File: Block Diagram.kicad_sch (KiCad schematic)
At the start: 48 parts, among them J1001 Header, J701 ZHOURI DC3, J801 Molex 430452427, J901 Header

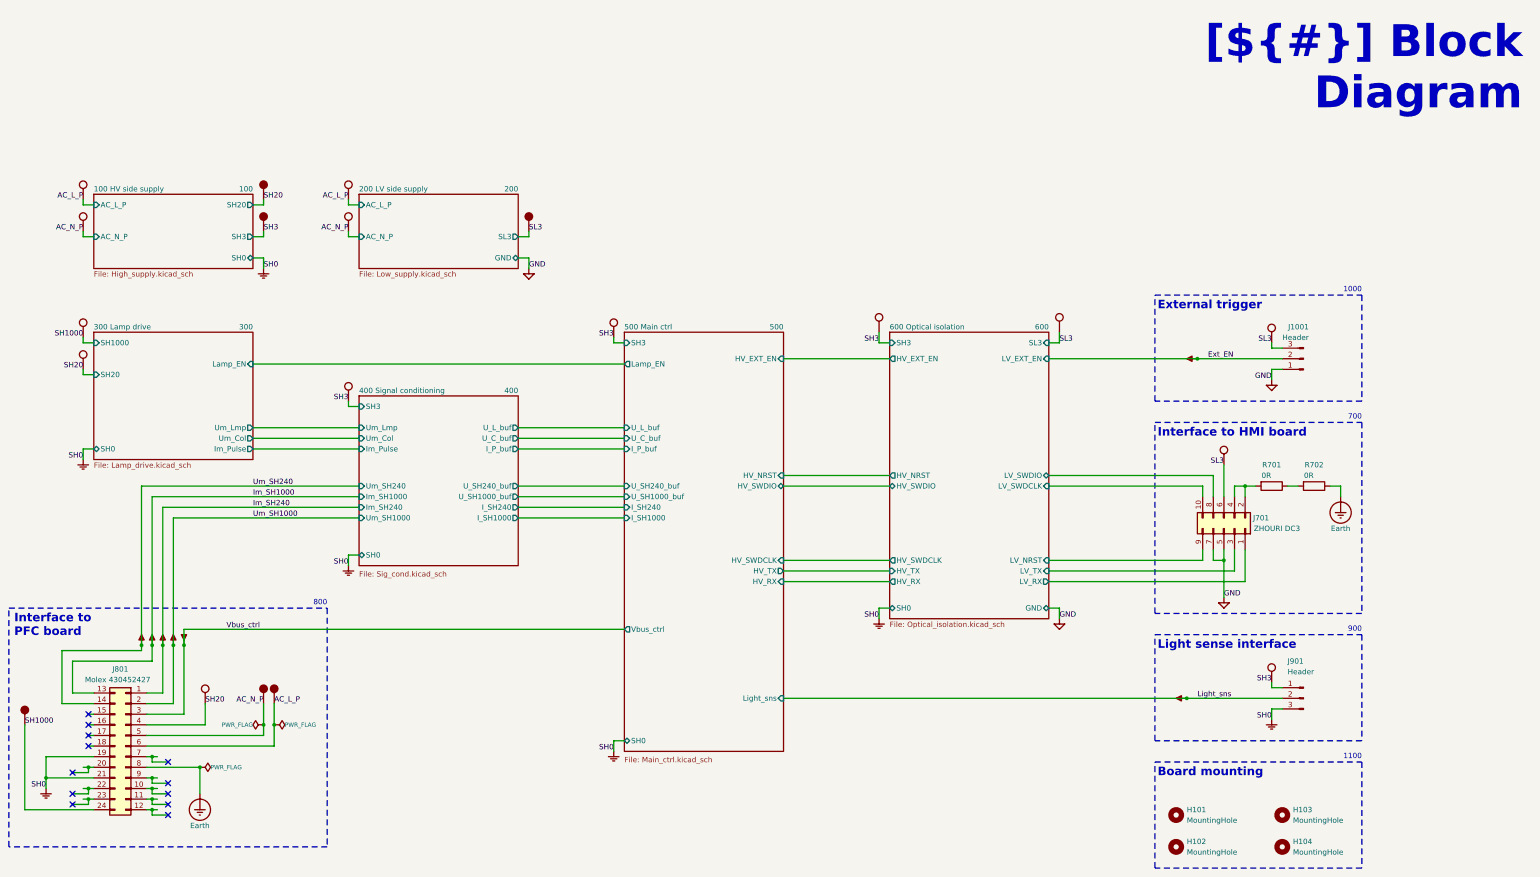
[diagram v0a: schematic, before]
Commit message: Reworked sheet titles
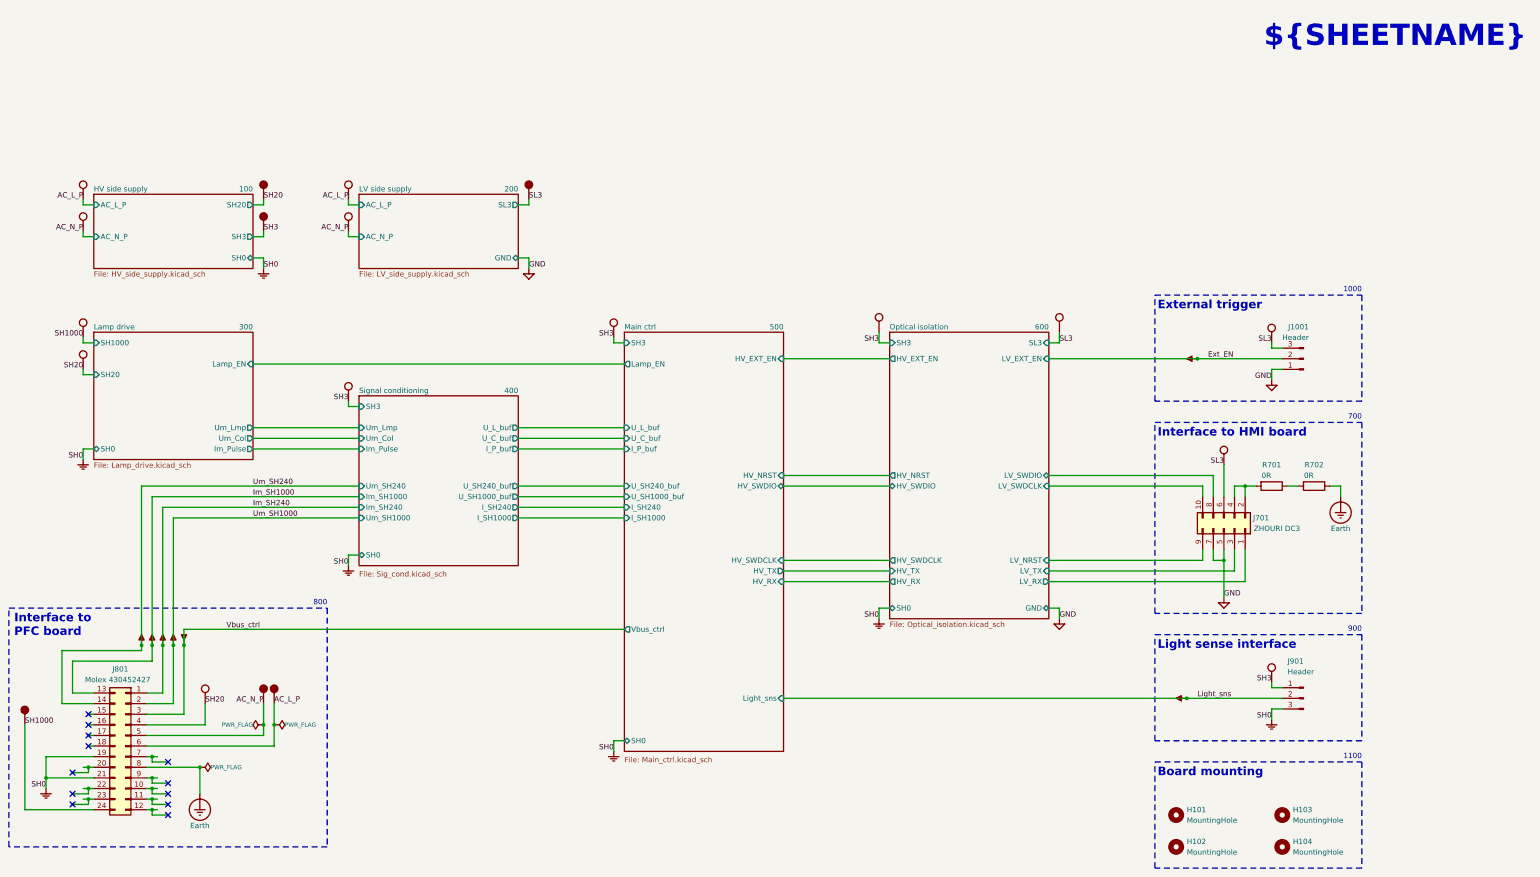
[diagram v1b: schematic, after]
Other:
- sheet 100 HV side supply renamed HV side supply
- sheet 200 LV side supply renamed LV side supply
- sheet 300 Lamp drive renamed Lamp drive
- sheet 400 Signal conditioning renamed Signal conditioning
- sheet 500 Main ctrl renamed Main ctrl
- sheet 600 Optical isolation renamed Optical isolation
- sheet HV side supply: file High_supply.kicad_sch -> HV_side_supply.kicad_sch
- sheet LV side supply: file Low_supply.kicad_sch -> LV_side_supply.kicad_sch
- title: Block Diagram -> ${SHEETNAME}
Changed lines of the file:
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@@
 	(paper "A3")
 	(title_block
-		(title "Block Diagram")
+		(title "${SHEETNAME}")
 		(date "2025-01-12")
 		(rev "${REVISION}")
@@
 		)
 	)
-	(text_box "[${#}] ${TITLE}"
+	(text_box "${SHEETNAME}"
 		(exclude_from_sim no)
-		(at 304.8 20.32 0)
-		(size 101.6 12.7)
-		(margins 5.9999 5.9999 5.9999 5.9999)
+		(at 350.52 15.24 0)
+		(size 53.34 7.62)
+		(margins 2.54 1.27 2.54 1.27)
 		(stroke
 			(width -0.0001)
@@
 			(font
 				(face "Times New Roman")
-				(size 7.62 7.62)
+				(size 5.08 5.08)
 				(thickness 1.2)
 				(bold yes)
@@
 	(wire
 		(pts
-			(xy 160.02 67.31) (xy 162.56 67.31)
+			(xy 160.02 59.69) (xy 162.56 59.69)
 		)
 		(stroke
@@
 	(wire
 		(pts
-			(xy 162.56 66.04) (xy 162.56 67.31)
+			(xy 162.56 58.42) (xy 162.56 59.69)
 		)
 		(stroke
@@
 	)
 	(label "SL3"
-		(at 162.56 66.04 0)
+		(at 162.56 58.42 0)
 		(effects
 			(font
@@
 	(symbol
 		(lib_id "personal:Cosmetic_PWR_SRC")
-		(at 162.56 66.04 0)
+		(at 162.56 58.42 0)
 		(mirror y)
 		(unit 1)
@@
 		(fields_autoplaced yes)
 		(property "Reference" "P787"
-			(at 162.56 60.706 0)
+			(at 162.56 53.086 0)
 			(do_not_autoplace yes)
 			(effects
@@
 		)
 		(property "Value" "~"
-			(at 162.56 59.69 90)
+			(at 162.56 52.07 90)
 			(effects
 				(font
@@
 		)
 		(property "Footprint" ""
-			(at 162.56 66.04 0)
+			(at 162.56 58.42 0)
 			(effects
 				(font
@@
 		)
 		(property "Datasheet" ""
-			(at 162.56 66.04 0)
+			(at 162.56 58.42 0)
 			(effects
 				(font
@@
 		)
 		(property "Description" ""
-			(at 162.56 66.04 0)
+			(at 162.56 58.42 0)
 			(effects
 				(font
@@
 			(color 255 220 210 1.0000)
 		)
-		(property "Sheetname" "400 Signal conditioning"
+		(property "Sheetname" "Signal conditioning"
 			(at 121.92 104.14 0)
 			(effects
@@
 			)
 		)
-		(property "Range" "400"
+		(property "RefDes" "400"
 			(at 160.02 104.14 0)
 			(effects
@@
 			(color 255 220 210 1.0000)
 		)
-		(property "Sheetname" "300 Lamp drive"
+		(property "Sheetname" "Lamp drive"
 			(at 58.42 88.9 0)
 			(effects
@@
 			)
 		)
-		(property "Range" "300"
+		(property "RefDes" "300"
 			(at 96.52 88.9 0)
 			(effects
@@
 			(color 255 220 210 1.0000)
 		)
-		(property "Sheetname" "600 Optical isolation"
+		(property "Sheetname" "Optical isolation"
 			(at 248.92 88.9 0)
 			(effects
@@
 			)
 		)
-		(property "Range" "600"
+		(property "RefDes" "600"
 			(at 287.02 88.9 0)
 			(effects
@@
 			(color 255 220 210 1.0000)
 		)
-		(property "Sheetname" "200 LV side supply"
+		(property "Sheetname" "LV side supply"
 			(at 121.92 55.88 0)
 			(effects
@@
 			)
 		)
-		(property "Sheetfile" "Low_supply.kicad_sch"
+		(property "Sheetfile" "LV_side_supply.kicad_sch"
 			(at 121.92 75.5146 0)
 			(effects
@@
 			)
 		)
-		(property "Range" "200"
+		(property "RefDes" "200"
 			(at 160.02 55.88 0)
 			(effects
@@
 		)
 		(pin "SL3" output
-			(at 160.02 67.31 0)
+			(at 160.02 59.69 0)
 			(effects
 				(font
@@
 			(color 255 220 210 1.0000)
 		)
-		(property "Sheetname" "100 HV side supply"
+		(property "Sheetname" "HV side supply"
 			(at 58.42 55.88 0)
 			(effects
@@
 			)
 		)
-		(property "Sheetfile" "High_supply.kicad_sch"
+		(property "Sheetfile" "HV_side_supply.kicad_sch"
 			(at 58.42 75.5146 0)
 			(effects
@@
 			)
 		)
-		(property "Range" "100"
+		(property "RefDes" "100"
 			(at 96.52 55.88 0)
 			(effects
@@
 			(color 255 220 210 1.0000)
 		)
-		(property "Sheetname" "500 Main ctrl"
+		(property "Sheetname" "Main ctrl"
 			(at 185.42 88.9 0)
 			(effects
@@
 			)
 		)
-		(property "Range" "500"
+		(property "RefDes" "500"
 			(at 223.52 88.9 0)
 			(effects

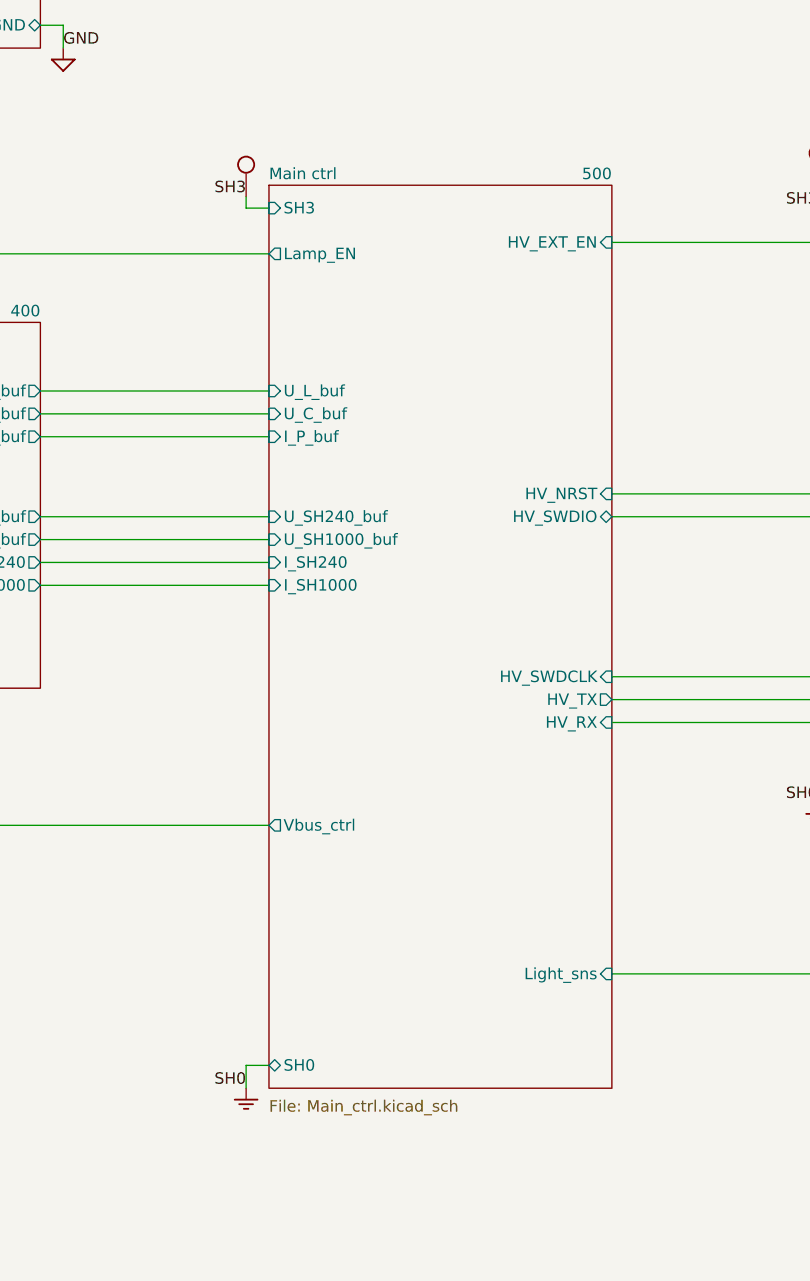
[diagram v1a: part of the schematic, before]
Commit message: Reworked sheet titles and changelog
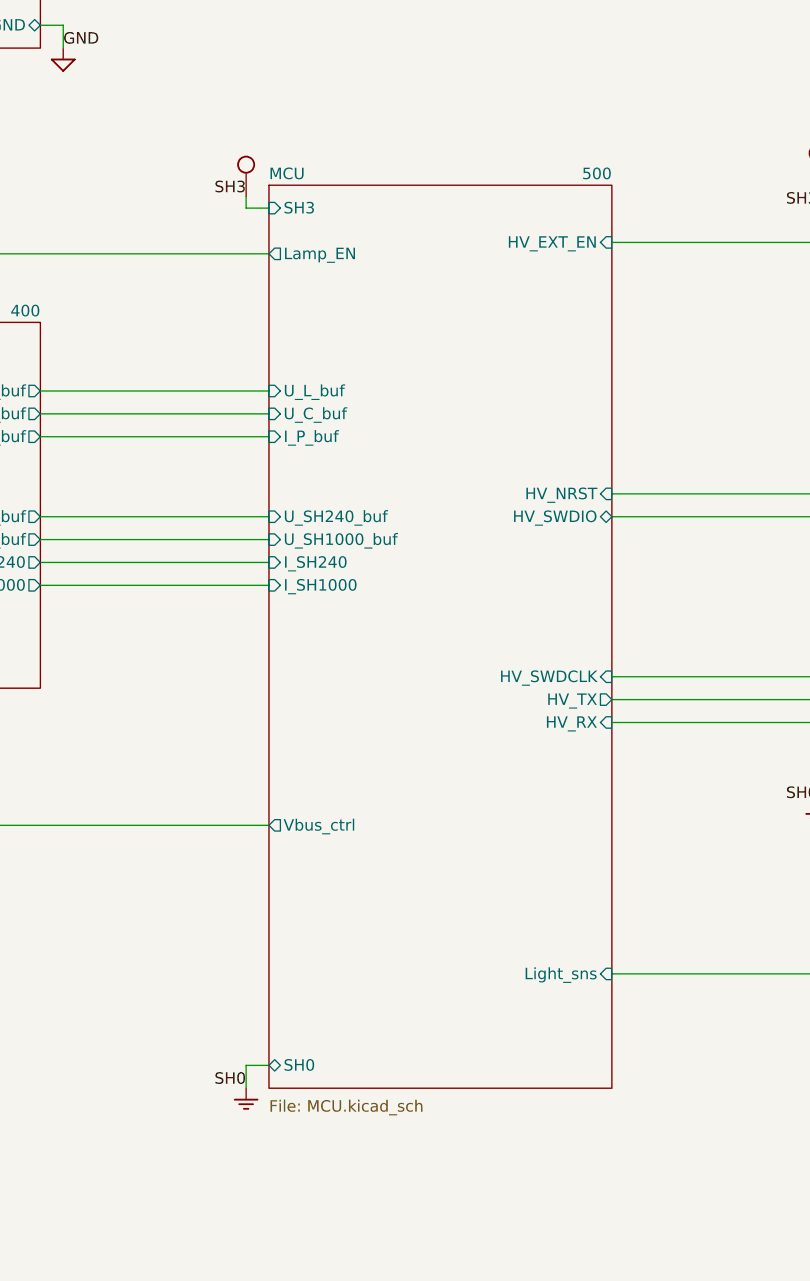
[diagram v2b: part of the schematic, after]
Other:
- sheet Main ctrl renamed MCU
- sheet MCU: file Main_ctrl.kicad_sch -> MCU.kicad_sch
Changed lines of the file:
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@@
 			(color 255 220 210 1.0000)
 		)
-		(property "Sheetname" "Main ctrl"
+		(property "Sheetname" "MCU"
 			(at 185.42 88.9 0)
 			(effects
@@
 			)
 		)
-		(property "Sheetfile" "Main_ctrl.kicad_sch"
+		(property "Sheetfile" "MCU.kicad_sch"
 			(at 185.42 191.77 0)
 			(effects

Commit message: Added PCB
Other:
- sheet Lamp drive renamed Lamp driver
- sheet Lamp driver: file Lamp_drive.kicad_sch -> Lamp_driver.kicad_sch
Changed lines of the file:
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@@
 	(title_block
 		(title "${SHEETNAME}")
-		(date "2025-01-12")
+		(date "2025-07-04")
 		(rev "${REVISION}")
 		(company "${COMPANY}")
@@
 		(at 350.52 15.24 0)
 		(size 53.34 7.62)
-		(margins 2.54 1.27 2.54 1.27)
+		(margins 1.27 1.27 1.27 1.27)
 		(stroke
 			(width -0.0001)
@@
 	)
 	(junction
+		(at 41.91 189.23)
+		(diameter 0)
+		(color 0 0 0 0)
+	)
+	(junction
 		(at 77.47 165.1)
 		(diameter 0)
@@
 	(wire
 		(pts
-			(xy 41.91 184.15) (xy 41.91 204.47)
+			(xy 41.91 184.15) (xy 41.91 189.23)
 		)
 		(stroke
@@
 	(wire
 		(pts
+			(xy 41.91 189.23) (xy 41.91 204.47)
+		)
+		(stroke
+			(width 0)
+			(type default)
+		)
+	)
+	(wire
+		(pts
 			(xy 287.02 127) (xy 323.85 127)
 		)
@@
 			)
 		)
-		(property "Description" ""
+		(property "Description" "Local power symbol (source), cosmetic use only"
 			(at 99.06 66.04 0)
 			(effects
@@
 	)
 	(symbol
-		(lib_name "Cosmetic_PWR_4")
 		(lib_id "personal:Cosmetic_PWR")
 		(at 55.88 58.42 0)
@@
 			)
 		)
-		(property "Description" ""
+		(property "Description" "Local power symbol (sink), cosmetic use only"
 			(at 55.88 58.42 0)
 			(effects
@@
 	)
 	(symbol
-		(lib_name "Cosmetic_PWR_4")
 		(lib_id "personal:Cosmetic_PWR")
 		(at 289.56 90.17 0)
@@
 			)
 		)
-		(property "Description" ""
+		(property "Description" "Local power symbol (sink), cosmetic use only"
 			(at 289.56 90.17 0)
 			(effects
@@
 	)
 	(symbol
-		(lib_name "Cosmetic_PWR_4")
 		(lib_id "personal:Cosmetic_PWR")
 		(at 119.38 58.42 0)
@@
 			)
 		)
-		(property "Description" ""
+		(property "Description" "Local power symbol (sink), cosmetic use only"
 			(at 119.38 58.42 0)
 			(effects
@@
 	)
 	(symbol
-		(lib_name "Cosmetic_PWR_4")
 		(lib_id "personal:Cosmetic_PWR")
 		(at 55.88 99.06 0)
@@
 			)
 		)
-		(property "Description" ""
+		(property "Description" "Local power symbol (sink), cosmetic use only"
 			(at 55.88 99.06 0)
 			(effects
@@
 			)
 		)
-		(property "Description" ""
+		(property "Description" "Local power symbol (sink), cosmetic use only"
 			(at 340.36 92.71 0)
 			(effects
@@
 			)
 		)
-		(property "Description" ""
+		(property "Description" "Local power symbol (source), cosmetic use only"
 			(at 99.06 58.42 0)
 			(effects
@@
 			)
 		)
-		(property "Description" ""
+		(property "Description" "Local power symbol (source), cosmetic use only"
 			(at 99.06 179.07 0)
 			(effects
@@
 			)
 		)
-		(property "Description" ""
+		(property "Description" "Local power symbol (source), cosmetic use only"
 			(at 101.6 179.07 0)
 			(effects
@@
 	)
 	(symbol
-		(lib_name "Cosmetic_PWR_4")
+		(lib_id "power:PWR_FLAG")
+		(at 41.91 189.23 270)
+		(unit 1)
+		(exclude_from_sim no)
+		(in_bom yes)
+		(on_board yes)
+		(dnp no)
+		(property "Reference" "#FLG02"
+			(at 43.815 189.23 0)
+			(effects
+				(font
+					(size 1.27 1.27)
+				)
+				(hide yes)
+			)
+		)
+		(property "Value" "PWR_FLAG"
+			(at 44.45 189.23 90)
+			(effects
+				(font
+					(size 1.016 1.016)
+				)
+				(justify left)
+			)
+		)
+		(property "Footprint" ""
+			(at 41.91 189.23 0)
+			(effects
+				(font
+					(size 1.27 1.27)
+				)
+				(hide yes)
+			)
+		)
+		(property "Datasheet" "~"
+			(at 41.91 189.23 0)
+			(effects
+				(font
+					(size 1.27 1.27)
+				)
+				(hide yes)
+			)
+		)
+		(property "Description" "Special symbol for telling ERC where power comes from"
+			(at 41.91 189.23 0)
+			(effects
+				(font
+					(size 1.27 1.27)
+				)
+				(hide yes)
+			)
+		)
+		(pin "1"
+		)
+		(instances
+			(project "Strobe_main"
+				(path "/f9e05184-c88b-4a88-ae9c-ab2bdb32be7c/82da9dbf-ba38-4d08-ba35-a220fa2963b1"
+					(reference "#FLG02")
+					(unit 1)
+				)
+			)
+		)
+	)
+	(symbol
 		(lib_id "personal:Cosmetic_PWR")
 		(at 85.09 179.07 0)
@@
 			)
 		)
-		(property "Description" ""
+		(property "Description" "Local power symbol (sink), cosmetic use only"
 			(at 85.09 179.07 0)
 			(effects
@@
 	)
 	(symbol
-		(lib_name "Cosmetic_PWR_4")
 		(lib_id "personal:Cosmetic_PWR")
 		(at 55.88 66.04 0)
@@
 			)
 		)
-		(property "Description" ""
+		(property "Description" "Local power symbol (sink), cosmetic use only"
 			(at 55.88 66.04 0)
 			(effects
@@
 			)
 		)
-		(property "Description" ""
+		(property "Description" "Local power symbol (source), cosmetic use only"
 			(at 41.91 184.15 0)
 			(effects
@@
 	)
 	(symbol
-		(lib_name "Cosmetic_PWR_4")
 		(lib_id "personal:Cosmetic_PWR")
 		(at 328.93 121.92 0)
@@
 			)
 		)
-		(property "Description" ""
+		(property "Description" "Local power symbol (sink), cosmetic use only"
 			(at 328.93 121.92 0)
 			(effects
@@
 	)
 	(symbol
-		(lib_name "Cosmetic_PWR_4")
 		(lib_id "personal:Cosmetic_PWR")
 		(at 119.38 66.04 0)
@@
 			)
 		)
-		(property "Description" ""
+		(property "Description" "Local power symbol (sink), cosmetic use only"
 			(at 119.38 66.04 0)
 			(effects
@@
 			)
 		)
-		(property "Description" ""
+		(property "Description" "Local power symbol (source), cosmetic use only"
 			(at 162.56 58.42 0)
 			(effects
@@
 			)
 		)
-		(property "Description" ""
+		(property "Description" "Local power symbol (sink), cosmetic use only"
 			(at 340.36 173.99 0)
 			(effects
@@
 	)
 	(symbol
-		(lib_name "Cosmetic_PWR_4")
 		(lib_id "personal:Cosmetic_PWR")
 		(at 55.88 91.44 0)
@@
 			)
 		)
-		(property "Description" ""
+		(property "Description" "Local power symbol (sink), cosmetic use only"
 			(at 55.88 91.44 0)
 			(effects
@@
 	)
 	(symbol
-		(lib_name "Cosmetic_PWR_4")
 		(lib_id "personal:Cosmetic_PWR")
 		(at 119.38 106.68 0)
@@
 			)
 		)
-		(property "Description" ""
+		(property "Description" "Local power symbol (sink), cosmetic use only"
 			(at 119.38 106.68 0)
 			(effects
@@
 	)
 	(symbol
-		(lib_name "Cosmetic_PWR_4")
 		(lib_id "personal:Cosmetic_PWR")
 		(at 246.38 90.17 0)
@@
 			)
 		)
-		(property "Description" ""
+		(property "Description" "Local power symbol (sink), cosmetic use only"
 			(at 246.38 90.17 0)
 			(effects
@@
 	)
 	(symbol
-		(lib_name "Cosmetic_PWR_4")
 		(lib_id "personal:Cosmetic_PWR")
 		(at 182.88 91.44 0)
@@
 			)
 		)
-		(property "Description" ""
+		(property "Description" "Local power symbol (sink), cosmetic use only"
 			(at 182.88 91.44 0)
 			(effects
@@
 			(color 255 220 210 1.0000)
 		)
-		(property "Sheetname" "Lamp drive"
+		(property "Sheetname" "Lamp driver"
 			(at 58.42 88.9 0)
 			(effects
@@
 			)
 		)
-		(property "Sheetfile" "Lamp_drive.kicad_sch"
+		(property "Sheetfile" "Lamp_driver.kicad_sch"
 			(at 58.42 121.285 0)
 			(effects

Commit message: updating BOM info
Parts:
- J1001, J901, R701, R702: Manufacturer (none) -> Generic
- J701: Field5 https://www.lcsc.com/product-detail/IDC-Connectors_ZHOURI-D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 -> (none); Manufacturer (none) -> ZHOURI; Manufacturer Part Number (none) -> DC3-2.54-10PAS
- J801: Manufacturer (none) -> Molex; Manufacturer Part Number (none) -> 430452427
